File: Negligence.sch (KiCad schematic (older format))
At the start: 112 parts, among them J1 AVR-ISP-6, SW1 keyboard_parts_KEYSW, SW10 keyboard_parts_KEYSW, SW11 keyboard_parts_KEYSW, SW12 keyboard_parts_KEYSW, SW13 keyboard_parts_KEYSW, SW14 keyboard_parts_KEYSW, SW15 keyboard_parts_KEYSW, SW16 keyboard_parts_KEYSW, SW17 keyboard_parts_KEYSW, SW18 keyboard_parts_KEYSW, SW19 keyboard_parts_KEYSW, SW2 keyboard_parts_KEYSW, SW20 keyboard_parts_KEYSW, SW21 keyboard_parts_KEYSW, SW22 keyboard_parts_KEYSW, SW23 keyboard_parts_KEYSW, SW24 keyboard_parts_KEYSW, SW25 keyboard_parts_KEYSW, SW26 keyboard_parts_KEYSW, SW27 keyboard_parts_KEYSW, SW28 keyboard_parts_KEYSW, SW29 keyboard_parts_KEYSW, SW3 keyboard_parts_KEYSW, SW30 keyboard_parts_KEYSW, SW31 keyboard_parts_KEYSW, SW32 keyboard_parts_KEYSW, SW33 keyboard_parts_KEYSW, SW34 keyboard_parts_KEYSW, SW35 keyboard_parts_KEYSW, SW36 keyboard_parts_KEYSW, SW37 keyboard_parts_KEYSW, SW38 keyboard_parts_KEYSW, SW39 keyboard_parts_KEYSW, SW4 keyboard_parts_KEYSW, SW40 keyboard_parts_KEYSW, SW41 keyboard_parts_KEYSW, SW42 keyboard_parts_KEYSW, SW43 keyboard_parts_KEYSW, SW44 keyboard_parts_KEYSW, SW45 keyboard_parts_KEYSW, SW46 keyboard_parts_KEYSW, SW47 SW_Push, SW48 SW_Push, SW5 keyboard_parts_KEYSW, SW6 keyboard_parts_KEYSW, SW7 keyboard_parts_KEYSW, SW8 keyboard_parts_KEYSW, SW9 keyboard_parts_KEYSW, U1 ATmega328P-PU, Y1 16MHz

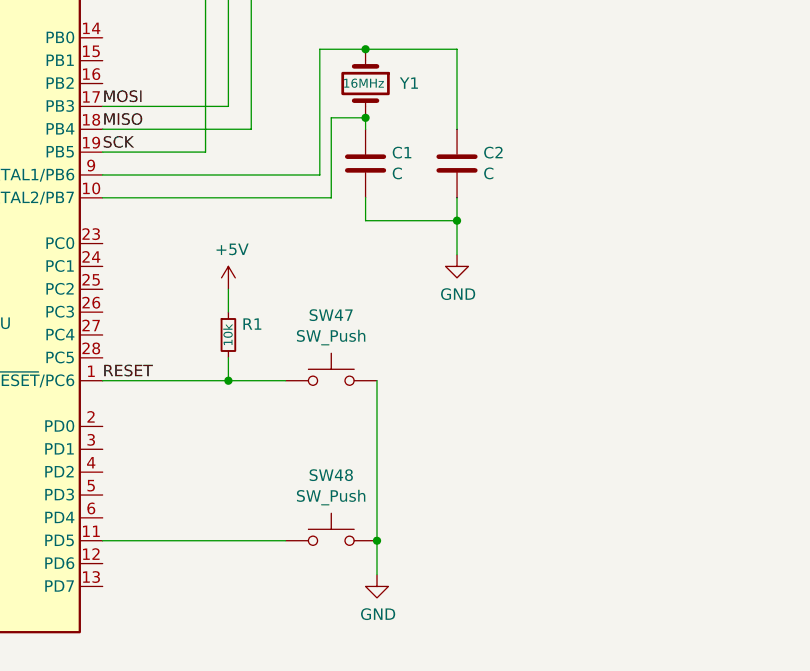
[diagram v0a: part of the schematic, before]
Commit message: Layout switches on pcb
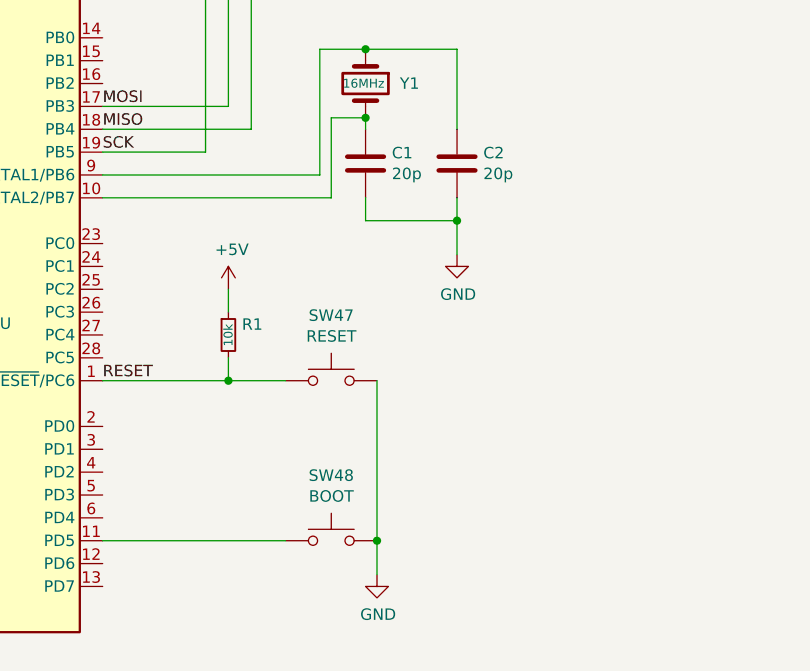
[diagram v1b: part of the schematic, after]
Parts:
- C1, C2: value C -> 20p; footprint (none) -> cftkb:D_DO-35_SOD27_P5.08mm_Horizontal
- C3, C4, C5, D47, D48: footprint (none) -> cftkb:D_DO-35_SOD27_P5.08mm_Horizontal
- D1, D10, D11, D12, D13, D14, D15, D16, D17, D18, D19, D2, D20, D21, D22, D23, D24, D25, D26, D27, D28, D29, D3, D30, D31, D32, D33, D34, D35, D36, D37, D38, D39, D4, D40, D41, D42, D43, D44, D45, D46, D5, D6, D7, D8, D9: footprint Diode_THT:D_DO-35_SOD27_P7.62mm_Horizontal -> cftkb:D_DO-35_SOD27_P5.08mm_Horizontal
- F1: footprint (none) -> cftkb:polyfuse_5.1mm
- J1: footprint (none) -> cftkb:AVR_ICSP_3x2
- R1, R2, R3, R4, R5, R6: footprint (none) -> cftkb:R_Axial_DIN0204_L3.6mm_D1.6mm_P7.62mm_Horizontal
- SW1, SW10, SW11, SW12, SW13, SW14, SW15, SW16, SW17, SW18, SW19, SW2, SW20, SW21, SW22, SW23, SW24, SW25, SW26, SW27, SW28, SW29, SW3, SW30, SW31, SW32, SW33, SW34, SW35, SW36, SW37, SW38, SW39, SW4, SW40, SW43, SW44, SW45, SW46, SW5, SW6, SW7, SW8, SW9: footprint (none) -> cftkb:SW_Cherry_MX1A_1.00u_PCB-NOSCREEN
- SW41, SW42: footprint (none) -> cftkb:SW_Cherry_MX1A_2.00u_PCBNOSCREEN
- SW47: value SW_Push -> RESET; footprint (none) -> cftkb:SW_PUSH_6mm
- SW48: value SW_Push -> BOOT; footprint (none) -> cftkb:SW_PUSH_6mm
- USB1: footprint (none) -> cftkb:USB_C_GCT_USB4085
- Y1: footprint (none) -> cftkb:Crystal_HC49-4H_Vertical

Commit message: Start MCU wiring
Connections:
- net SCK is gone; now on net COL2: J1.3 (SCK), U1.19 (PB5)
- net COL10: now also U1.3 (PD1)
- net COL11: now also U1.2 (PD0)
- net COL3: now also U1.28 (PC5)
- net COL4: now also U1.27 (PC4)
- net COL5: now also U1.26 (PC3)
- net COL6: now also U1.25 (PC2)
- net COL7: now also U1.24 (PC1)
- net COL8: now also U1.23 (PC0)
- net COL9: now also U1.6 (PD4)
- net D+: now also U1.4 (PD2)
- net D-: now also U1.5 (PD3)
- net MISO: no longer names the net of J1.1 (MISO), U1.18 (PB4)
- net MOSI: no longer names the net of J1.4 (MOSI), U1.17 (PB3)

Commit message: Finish mcu
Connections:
- net COL0: now also J1.4 (MOSI), U1.17 (PB3)
- net COL1: now also J1.1 (MISO), U1.18 (PB4)
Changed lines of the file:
@@
 Text Label 6900 6450 0    50   ~ 0
 COL3
-Text Label 6900 5550 0    50   ~ 0
-COL2
 Text Label 6900 6950 0    50   ~ 0
 D+
 Text Label 6900 7050 0    50   ~ 0
 D-
+Text Label 6900 5450 0    50   ~ 0
+COL1
+Text Label 6900 5550 0    50   ~ 0
+COL2
+Text Label 6900 5350 0    50   ~ 0
+COL0
 $EndSCHEMATC

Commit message: Edge cuts and place components on board
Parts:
- C3: footprint cftkb:D_DO-35_SOD27_P5.08mm_Horizontal -> cftkb:CP_Radial_D4.0mm_P1.50mm
- C4, C5: footprint cftkb:D_DO-35_SOD27_P5.08mm_Horizontal -> cftkb:C_Disc_D4.3mm_W1.9mm_P5.00mm
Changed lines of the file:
@@
 F 0 "C4" H 14500 6300 50  0000 L CNN
 F 1 "0.1u" H 14500 5800 50  0000 L CNN
-F 2 "cftkb:D_DO-35_SOD27_P5.08mm_Horizontal" H 14588 5900 50  0001 C CNN
+F 2 "cftkb:C_Disc_D4.3mm_W1.9mm_P5.00mm" H 14588 5900 50  0001 C CNN
 F 3 "~" H 14550 6050 50  0001 C CNN
 	1    14550 6050
@@
 F 0 "C5" H 14700 6300 50  0000 L CNN
 F 1 "0.1u" H 14700 5800 50  0000 L CNN
-F 2 "cftkb:D_DO-35_SOD27_P5.08mm_Horizontal" H 14788 5900 50  0001 C CNN
+F 2 "cftkb:C_Disc_D4.3mm_W1.9mm_P5.00mm" H 14788 5900 50  0001 C CNN
 F 3 "~" H 14750 6050 50  0001 C CNN
 	1    14750 6050
@@
 F 0 "C3" H 14300 6300 50  0000 L CNN
 F 1 "4.7u" H 14250 5800 50  0000 L CNN
-F 2 "cftkb:D_DO-35_SOD27_P5.08mm_Horizontal" H 14350 6050 50  0001 C CNN
+F 2 "cftkb:CP_Radial_D4.0mm_P1.50mm" H 14350 6050 50  0001 C CNN
 F 3 "~" H 14350 6050 50  0001 C CNN
 	1    14350 6050

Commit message: Wire USB, various
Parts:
- C1, C2: footprint cftkb:D_DO-35_SOD27_P5.08mm_Horizontal -> cftkb:C_Disc_D3.0mm_W1.6mm_P2.50mm
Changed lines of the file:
@@
 F 0 "C1" H 8165 5646 50  0000 L CNN
 F 1 "20p" H 8165 5555 50  0000 L CNN
-F 2 "cftkb:D_DO-35_SOD27_P5.08mm_Horizontal" H 8088 5450 50  0001 C CNN
+F 2 "cftkb:C_Disc_D3.0mm_W1.6mm_P2.50mm" H 8088 5450 50  0001 C CNN
 F 3 "~" H 8050 5600 50  0001 C CNN
 	1    8050 5600
@@
 F 0 "C2" H 8565 5646 50  0000 L CNN
 F 1 "20p" H 8565 5555 50  0000 L CNN
-F 2 "cftkb:D_DO-35_SOD27_P5.08mm_Horizontal" H 8488 5450 50  0001 C CNN
+F 2 "cftkb:C_Disc_D3.0mm_W1.6mm_P2.50mm" H 8488 5450 50  0001 C CNN
 F 3 "~" H 8450 5600 50  0001 C CNN
 	1    8450 5600

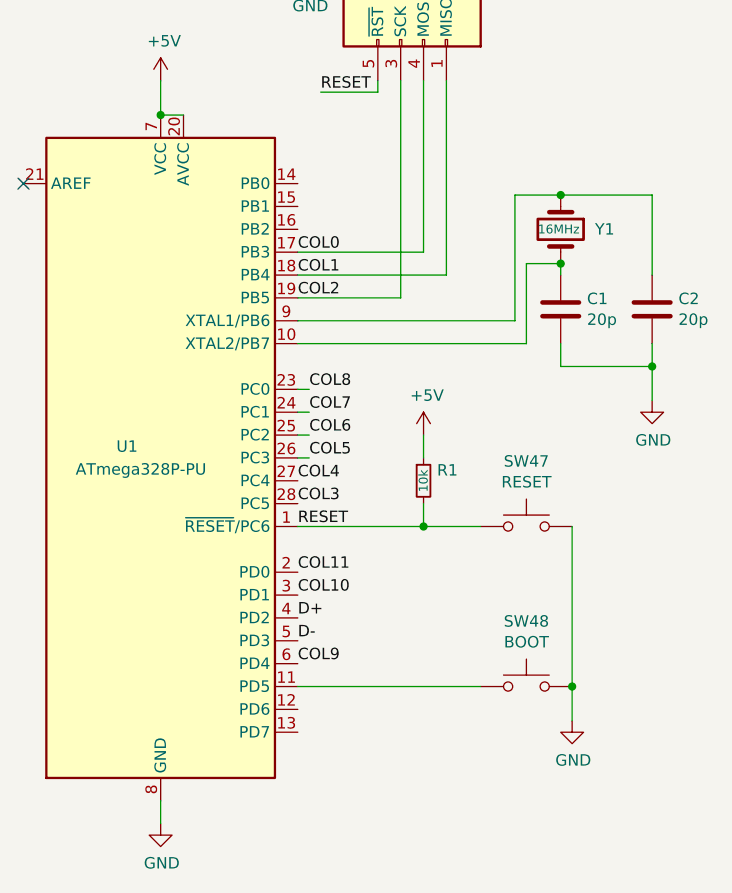
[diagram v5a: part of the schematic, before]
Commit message: Start diode rows
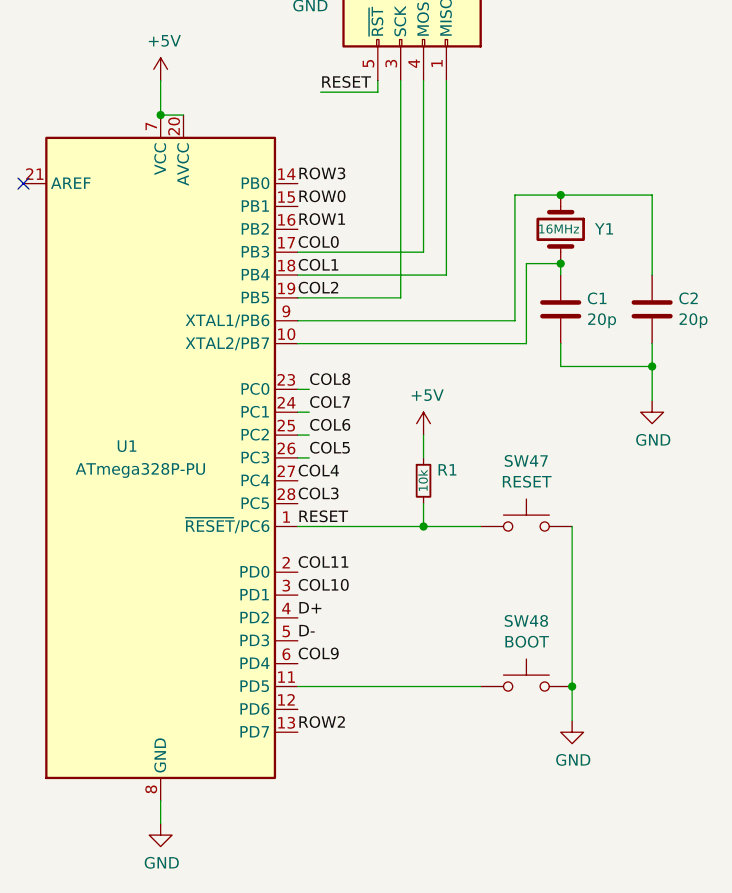
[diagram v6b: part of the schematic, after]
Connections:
- net ROW0: now also U1.15 (PB1)
- net ROW1: now also U1.16 (PB2)
- net ROW2: now also U1.13 (PD7)
- net ROW3: now also U1.14 (PB0)
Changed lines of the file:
@@
 Text Label 6900 5350 0    50   ~ 0
 COL0
+Text Label 6900 5150 0    50   ~ 0
+ROW0
+Text Label 6900 5250 0    50   ~ 0
+ROW1
+Text Label 6900 7450 0    50   ~ 0
+ROW2
+Text Label 6900 5050 0    50   ~ 0
+ROW3
 $EndSCHEMATC

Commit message: Fully wired
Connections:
- net ROW0: now also U1.13 (PD7); no longer U1.15 (PB1)
- net ROW1: now also U1.14 (PB0); no longer U1.16 (PB2)
- net ROW2: now also U1.16 (PB2); no longer U1.13 (PD7)
- net ROW3: now also U1.15 (PB1); no longer U1.14 (PB0)
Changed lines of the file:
@@
 Wire Wire Line
 	6950 6250 6900 6250
-Text Label 6950 5950 0    50   ~ 0
-COL8
-Text Label 6950 6050 0    50   ~ 0
-COL7
 Wire Wire Line
 	6950 5950 6900 5950
-Text Label 6950 6150 0    50   ~ 0
-COL6
-Text Label 6950 6250 0    50   ~ 0
-COL5
-Text Label 6900 6350 0    50   ~ 0
-COL4
-Text Label 6900 6450 0    50   ~ 0
-COL3
 Text Label 6900 6950 0    50   ~ 0
 D+
@@
 Text Label 6900 5350 0    50   ~ 0
 COL0
+Text Label 6900 5050 0    50   ~ 0
+ROW1
+Text Label 6900 5250 0    50   ~ 0
+ROW2
 Text Label 6900 5150 0    50   ~ 0
+ROW3
+Text Label 6900 6450 0    50   ~ 0
+COL3
+Text Label 6900 6350 0    50   ~ 0
+COL4
+Text Label 6950 6050 0    50   ~ 0
+COL7
+Text Label 6950 6150 0    50   ~ 0
+COL6
+Text Label 6950 5950 0    50   ~ 0
+COL8
+Text Label 6950 6250 0    50   ~ 0
+COL5
+Text Label 6900 7450 0    50   ~ 0
 ROW0
-Text Label 6900 5250 0    50   ~ 0
-ROW1
-Text Label 6900 7450 0    50   ~ 0
-ROW2
-Text Label 6900 5050 0    50   ~ 0
-ROW3
 $EndSCHEMATC

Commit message: CSV/gerber
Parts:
- added D49: LED_RGBA, LED_THT:LED_D5.0mm-4_RGB, symbol Device:LED_RGBA
- added R7, R8, R9: 220Ω, cftkb:R_Axial_DIN0204_L3.6mm_D1.6mm_P7.62mm_Horizontal, symbol Device:R_Small
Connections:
- net +5V: now also D49.4 (A)
- net GND: now also R7.2, R8.2, R9.2
- new net: D49.3 (BK), R9.1
- new net: D49.2 (GK), R8.1
- new net: D49.1 (RK), R7.1
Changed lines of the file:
@@
 Text Label 6900 7450 0    50   ~ 0
 ROW0
+$Comp
+L power:+5V #PWR016
+U 1 1 5F6FE958
+P 14550 8300
+F 0 "#PWR016" H 14550 8150 50  0001 C CNN
+F 1 "+5V" H 14565 8473 50  0000 C CNN
+F 2 "" H 14550 8300 50  0001 C CNN
+F 3 "" H 14550 8300 50  0001 C CNN
+	1    14550 8300
+	1    0    0    -1
+$EndComp
+Wire Wire Line
+	14200 8300 14550 8300
+$Comp
+L Device:R_Small R9
+U 1 1 5F717CE0
+P 13600 8500
+F 0 "R9" V 13650 8650 50  0000 C CNN
+F 1 "220Ω" V 13600 8500 31  0000 C CNN
+F 2 "cftkb:R_Axial_DIN0204_L3.6mm_D1.6mm_P7.62mm_Horizontal" H 13600 8500 50  0001 C CNN
+F 3 "~" H 13600 8500 50  0001 C CNN
+	1    13600 8500
+	0    1    1    0
+$EndComp
+Wire Wire Line
+	13700 8500 13800 8500
+$Comp
+L Device:R_Small R8
+U 1 1 5F78099C
+P 13600 8300
+F 0 "R8" V 13650 8450 50  0000 C CNN
+F 1 "220Ω" V 13600 8300 31  0000 C CNN
+F 2 "cftkb:R_Axial_DIN0204_L3.6mm_D1.6mm_P7.62mm_Horizontal" H 13600 8300 50  0001 C CNN
+F 3 "~" H 13600 8300 50  0001 C CNN
+	1    13600 8300
+	0    1    1    0
+$EndComp
+$Comp
+L Device:R_Small R7
+U 1 1 5F780E79
+P 13600 8100
+F 0 "R7" V 13650 8250 50  0000 C CNN
+F 1 "220Ω" V 13600 8100 31  0000 C CNN
+F 2 "cftkb:R_Axial_DIN0204_L3.6mm_D1.6mm_P7.62mm_Horizontal" H 13600 8100 50  0001 C CNN
+F 3 "~" H 13600 8100 50  0001 C CNN
+	1    13600 8100
+	0    1    1    0
+$EndComp
+Wire Wire Line
+	13700 8100 13800 8100
+Wire Wire Line
+	13700 8300 13800 8300
+$Comp
+L power:GND #PWR015
+U 1 1 5F7AE110
+P 13400 8600
+F 0 "#PWR015" H 13400 8350 50  0001 C CNN
+F 1 "GND" H 13405 8427 50  0000 C CNN
+F 2 "" H 13400 8600 50  0001 C CNN
+F 3 "" H 13400 8600 50  0001 C CNN
+	1    13400 8600
+	1    0    0    -1
+$EndComp
+Wire Wire Line
+	13400 8600 13400 8500
+Wire Wire Line
+	13400 8100 13500 8100
+Wire Wire Line
+	13500 8300 13400 8300
+Connection ~ 13400 8300
+Wire Wire Line
+	13400 8300 13400 8100
+Wire Wire Line
+	13500 8500 13400 8500
+Connection ~ 13400 8500
+Wire Wire Line
+	13400 8500 13400 8300
+$Comp
+L Device:LED_RGBA D49
+U 1 1 5F803903
+P 14000 8300
+F 0 "D49" H 14000 8797 50  0000 C CNN
+F 1 "LED_RGBA" H 14000 8706 50  0000 C CNN
+F 2 "LED_THT:LED_D5.0mm-4_RGB" H 14000 8250 50  0001 C CNN
+F 3 "~" H 14000 8250 50  0001 C CNN
+	1    14000 8300
+	1    0    0    -1
+$EndComp
 $EndSCHEMATC
